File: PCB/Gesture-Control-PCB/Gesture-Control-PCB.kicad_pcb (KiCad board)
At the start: 2 copper layers, 30.5 x 57.5 mm, 5 parts, among them J1 Jack-DC, J2 Conn_01x07_Female, U1 L7806CV, U2 LD1117V33, U3 NodeMCU1.0(ESP-12E)

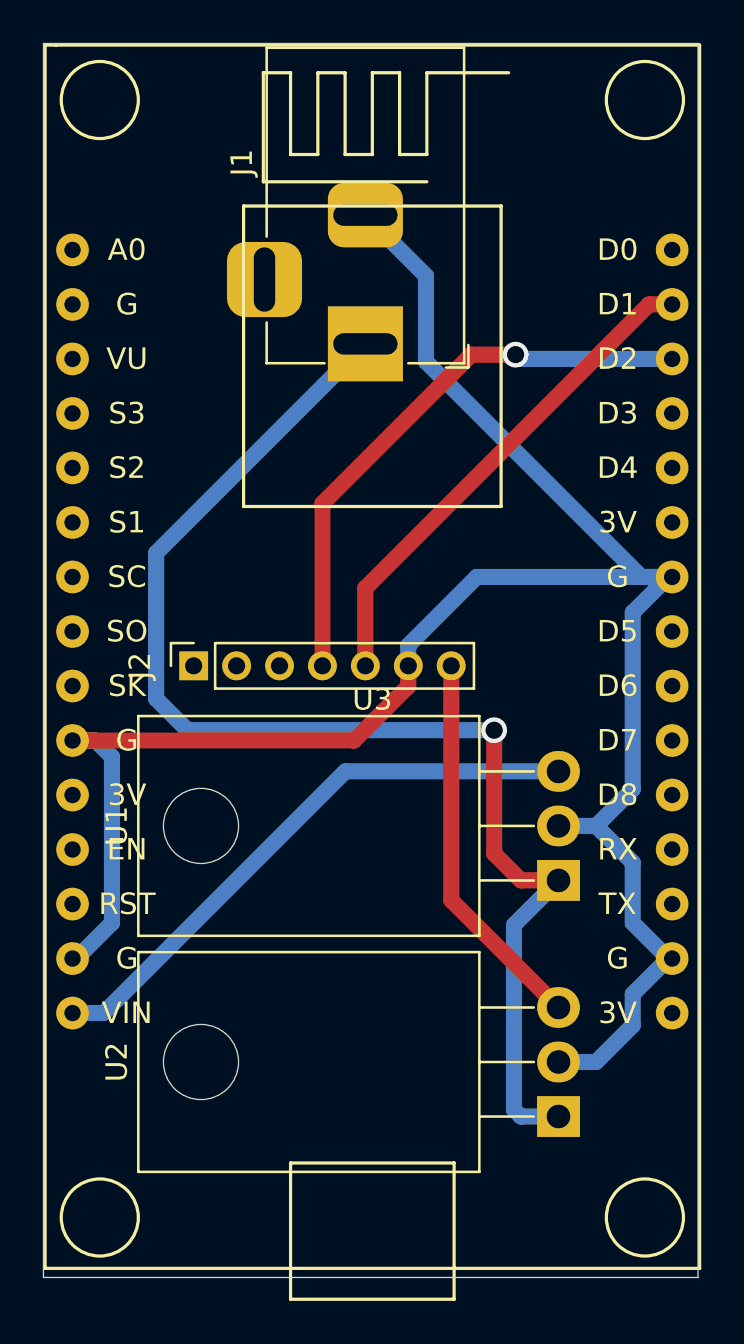
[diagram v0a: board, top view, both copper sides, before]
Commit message: removed one voltage regulator (lmao im a dummy)
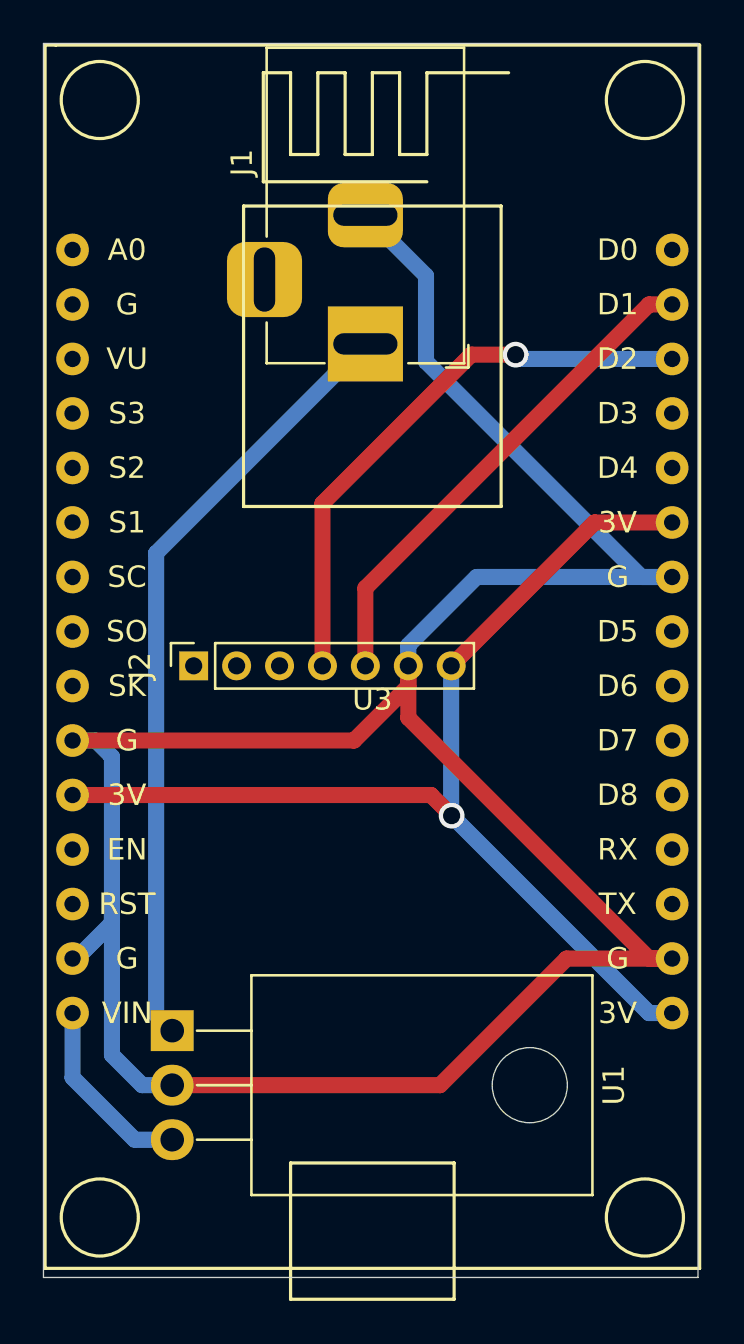
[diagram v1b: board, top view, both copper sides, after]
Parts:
- removed U2: LD1117V33, Package_TO_SOT_THT:TO-220-3_Horizontal_TabDown
- moved U1 19.3 mm to (92.0, 114.0), turned to 270 degrees
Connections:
- U3 pad 11: (no net) -> +3V3
- U3 pad 16: (no net) -> +3V3
- U3 pad 25: (no net) -> +3V3
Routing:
- net +3V3: track 18.0 -> 52.2 mm, vias 0 -> 1
- net GND: track 98.9 -> 123.7 mm
- net +12V: track 60.7 -> 36.3 mm, vias 1 -> 0
- net +6V: track 27.3 -> 8.85 mm

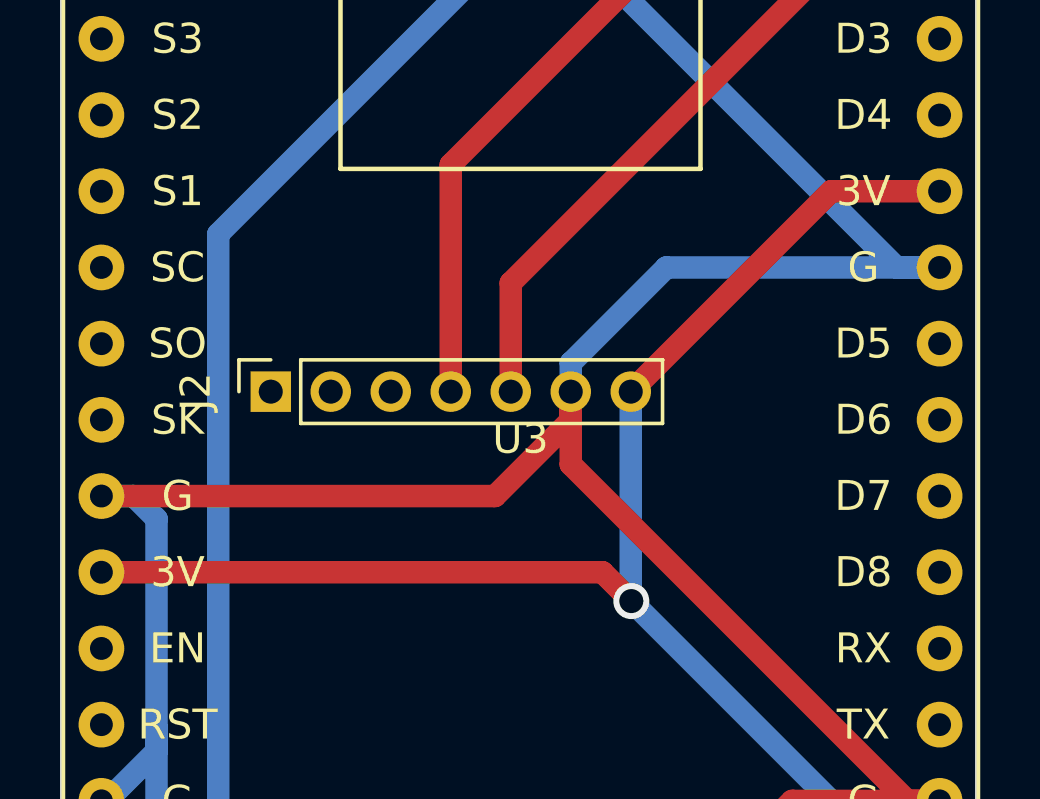
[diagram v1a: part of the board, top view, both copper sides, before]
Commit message: 3v3 only connected once instead of 3 times
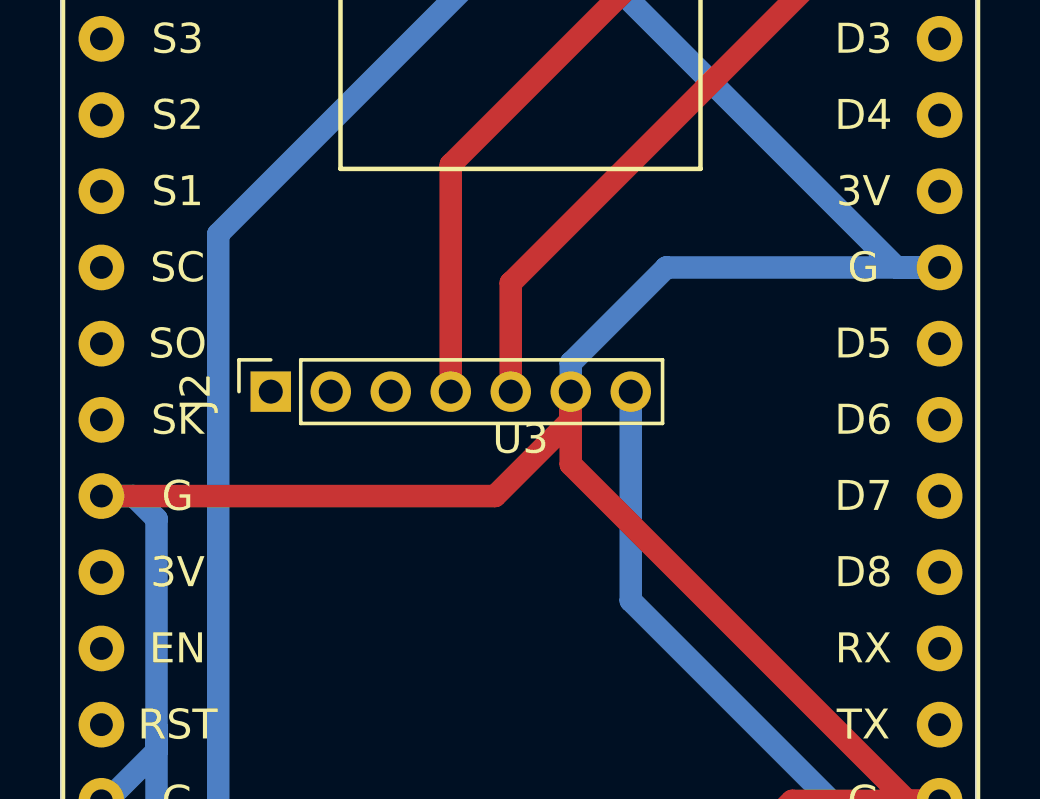
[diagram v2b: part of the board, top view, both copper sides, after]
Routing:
- net +3V3: track 52.2 -> 21.1 mm, vias 1 -> 0

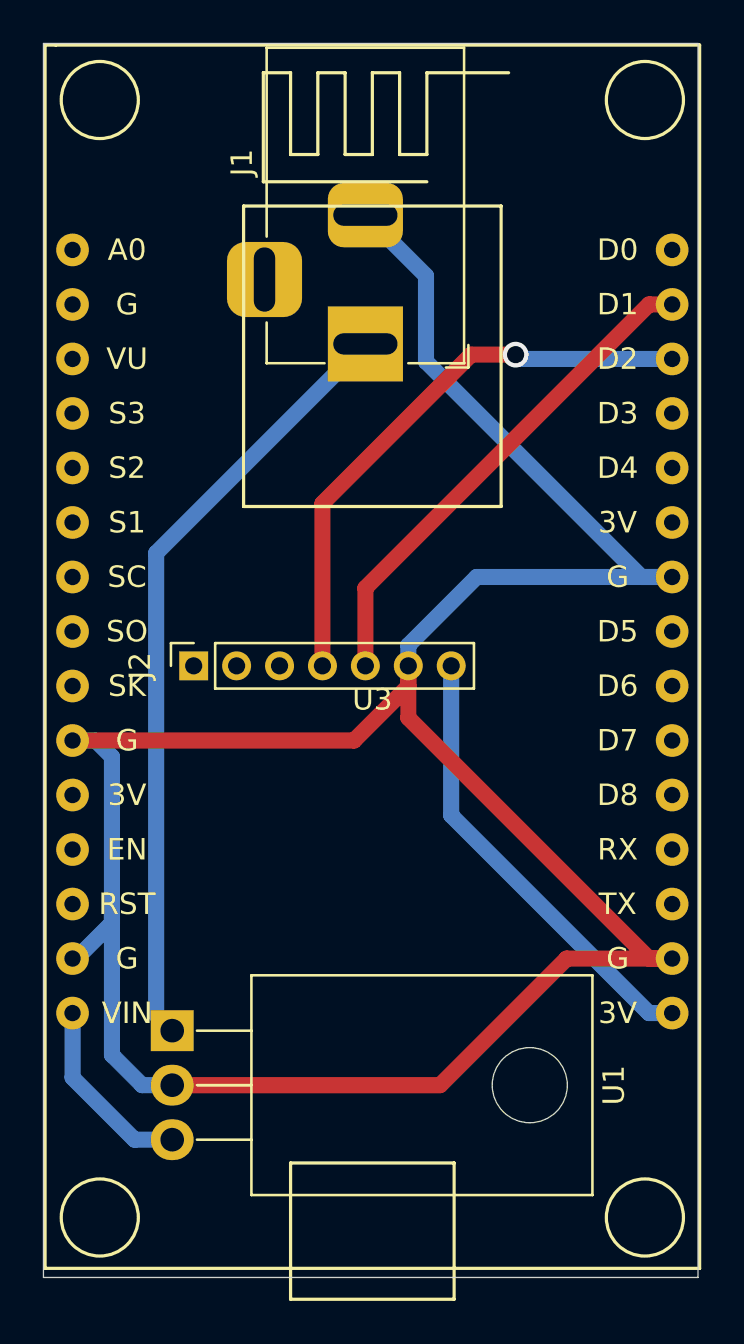
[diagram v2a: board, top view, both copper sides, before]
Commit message: fixed mpu socket and moved shit to bottom layer
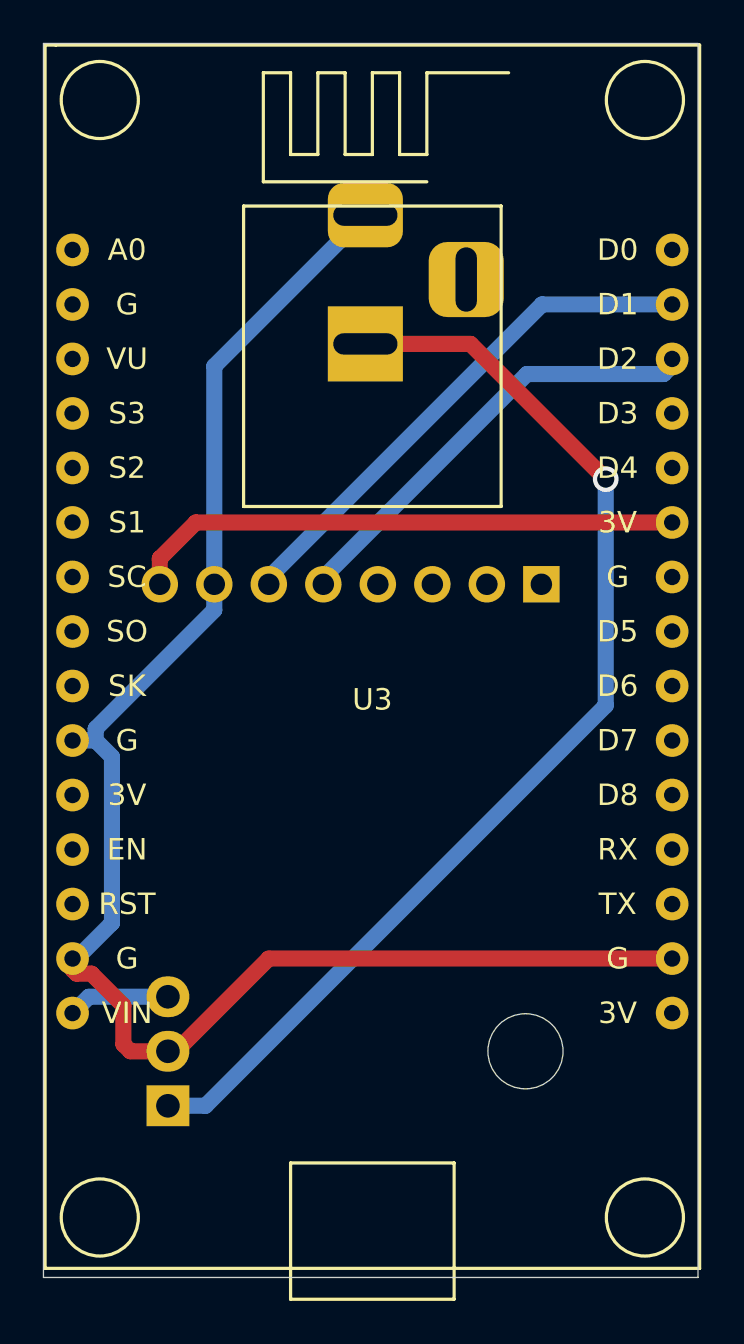
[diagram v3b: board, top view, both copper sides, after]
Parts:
- J1, U1: moved to B.Cu
- J2: value Conn_01x07_Female -> Conn_01x08_Female; footprint Connector_PinSocket_2.00mm:PinSocket_1x07_P2.00mm_Vertical -> Connector_PinSocket_2.54mm:PinSocket_1x08_P2.54mm_Vertical; moved to B.Cu
- moved J2 16.6 mm to (109.2, 93.2)
- moved U1 3.51 mm to (91.8, 117.5), turned to 90 degrees
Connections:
- J2 pad 4: /SDA -> (no net)
- J2 pad 5: /SCL -> /SDA
- J2 pad 6: GND -> /SCL
- J2 pad 7: +3V3 -> GND
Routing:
- net GND: track 123.7 -> 75.0 mm
- net +12V: track 36.3 -> 52.5 mm, vias 0 -> 1
- net /SDA: track 26.8 -> 21.0 mm, vias 1 -> 0
- net +3V3: track 21.1 -> 26.0 mm
- net +6V: track 8.85 -> 4.76 mm
- net /SCL: track 23.4 -> 24.4 mm
